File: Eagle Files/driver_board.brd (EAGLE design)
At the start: 127 x 114 mm, 70 parts, among them Q1 TIP32, Q2 TIP32, Q3 TIP32, Q4 TIP32, Q5 TIP32, Q6 TIP32, Q7 TIP32, Q8 TIP32, U1 STP16CPP05MTR, U10 STP16CPP05MTR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

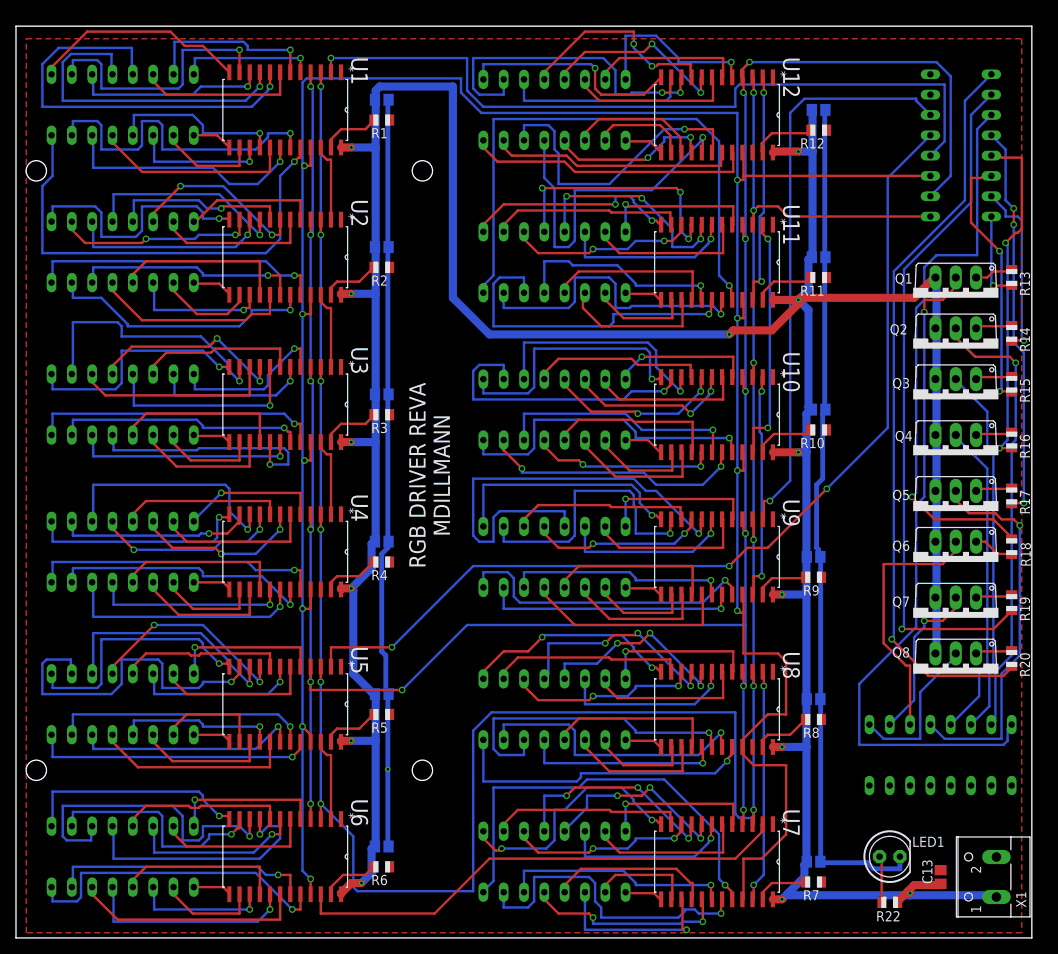
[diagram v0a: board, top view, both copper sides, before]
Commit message: Driver Board - Production Release
final board layout - release for production
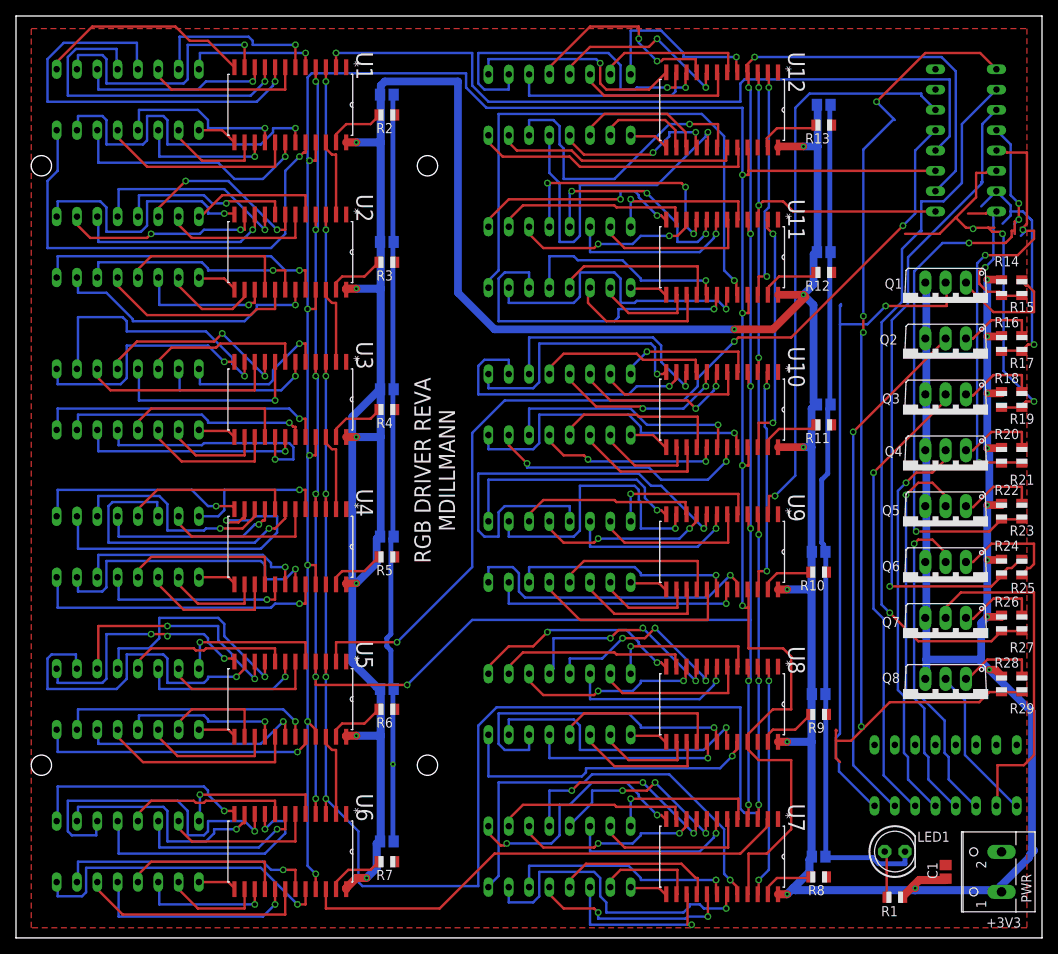
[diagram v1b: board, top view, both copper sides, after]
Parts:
- removed X1: (no value), con-wago-500:W237-102
- added PWR: (no value), con-wago-500:W237-102
- added R21, R23, R25, R27, R29: 1K, adafruit:R0805
- added R24, R26, R28: 2K, adafruit:R0805
- C1: value (none) -> 0.01
- R1: value 1K -> 220
- R13, R15, R17, R19: value 1k -> 1K
- R14, R16, R18, R20: value 1k -> 2K
- R22: value 220 -> 2K
- moved C1 119.5 mm to (116.2, 8.26), flipped to the top, turned to 90 degrees
- moved R1 116.4 mm to (109.9, 5.08), turned to 0 degrees
- moved C13 97.6 mm to (101.0, 104.1), flipped to the bottom, turned to 180 degrees
- moved SV14 78.8 mm to (116.2, 20.3), turned to 180 degrees
- moved SV13 76.9 mm to (118.7, 99.7), turned to 90 degrees
- moved C7 53.4 mm to (46.4, 12.1)
- moved R7 53.4 mm to (46.4, 9.53)
- moved R22 50.9 mm to (123.2, 53.3), turned to 270 degrees
- moved R13 30.2 mm to (101.0, 101.6), turned to 180 degrees
- moved R19 25.4 mm to (125.7, 67.3)
- moved R20 25.4 mm to (123.2, 60.3)
- moved C5 19.7 mm to (46.4, 50.2)
- moved C6 19.7 mm to (46.4, 31.1)
- moved C8 19.7 mm to (100.3, 10.2)
- moved R5 19.7 mm to (46.4, 47.6)
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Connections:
- net +3V3: now also PWR.1, R1.2, R14.1, R16.1, R18.1, R20.1, R22.1, R24.1, R26.1, R28.1; no longer R22.2, X1.1
- net CLK: now also SV13.2; no longer SV14.2
- net GND: now also PWR.2, R13.1; no longer R1.1, X1.2
- net LE: now also SV13.4; no longer SV14.4
- net N$108: now also R7.2; no longer R6.2
- net N$126: now also R8.2; no longer R7.2
- net N$144: now also R9.2; no longer R8.2
- net N$162: now also R10.2; no longer R9.2
- net N$180: now also R11.2; no longer R10.2
- net N$19: now also R2.2; no longer R1.2
- net N$198: now also R12.2; no longer R11.2
- net N$216: now also R13.2; no longer R12.2
- net N$226: now also SV14.1; no longer SV13.1
- net N$227: now also SV14.3; no longer SV13.3
- net N$228: now also SV14.5; no longer SV13.5
- net N$229: now also SV14.7; no longer SV13.7
- net N$230: now also SV14.9; no longer SV13.9
- net N$231: now also SV14.11; no longer SV13.11
- net N$232: now also R15.1; no longer R13.1
- net N$233: now also SV14.13; no longer SV13.13
- net N$234: now also SV14.15; no longer SV13.15
- net N$235: now also R29.1; no longer R20.1
- net N$236: now also R27.1; no longer R19.1
- net N$237: now also R25.1; no longer R18.1
- net N$238: now also R23.1; no longer R17.1
- net N$239: now also R21.1; no longer R16.1
- net N$240: now also R19.1; no longer R15.1
- net N$241: now also R17.1; no longer R14.1
- net N$243: now also R28.2, R29.2, SV13.15; no longer R20.2, SV14.15
- net N$244: now also R1.1; no longer R22.1
- net N$245: now also R26.2, R27.2, SV13.13; no longer R19.2, SV14.13
- net N$246: now also R24.2, R25.2, SV13.11; no longer R18.2, SV14.11
- net N$247: now also R22.2, R23.2, SV13.9; no longer R17.2, SV14.9
- net N$248: now also R20.2, R21.2, SV13.7; no longer R16.2, SV14.7
- net N$249: now also R18.2, R19.2, SV13.5; no longer R15.2, SV14.5
- net N$250: now also R16.2, R17.2, SV13.3; no longer R14.2, SV14.3
- net N$251: now also R14.2, R15.2, SV13.1; no longer R13.2, SV14.1
- net N$36: now also R3.2; no longer R2.2
- net N$54: now also R4.2; no longer R3.2
- net N$72: now also R5.2; no longer R4.2
- net N$90: now also R6.2; no longer R5.2
- net SDI_B: now also SV13.12; no longer SV14.12
- net SDI_G: now also SV13.10; no longer SV14.10
- net SDI_R: now also SV13.8; no longer SV14.8
- net ~OE: now also SV13.6; no longer SV14.6
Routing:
- net +3V3: track 432.1 -> 545.8 mm, vias 14 -> 22
- net N$243: track 93.2 -> 129.8 mm, vias 1 -> 4
- net N$247: track 49.3 -> 78.1 mm, vias 3 -> 4
- net N$233: track 20.6 -> 43.7 mm, vias 1 -> 0
- net N$249: track 32.6 -> 51.2 mm, vias 2 -> 3
- net N$149: track 24.5 -> 42.3 mm
- net N$145: track 21.3 -> 37.3 mm, vias 2 -> 1
- net N$246: track 69.5 -> 83.4 mm
- net N$248: track 43.3 -> 56.5 mm, vias 2 -> 3
- net N$228: track 46.4 -> 57.4 mm, vias 0 -> 1
- net N$229: track 39.7 -> 50.2 mm, vias 0 -> 1
- net N$232: track 5.00 -> 15.1 mm
- net N$231: track 32.6 -> 42.1 mm, vias 0 -> 1
- net N$251: track 11.0 -> 20.2 mm
- net N$227: track 56.5 -> 65.6 mm
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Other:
- board size 127 x 114 mm -> 128.2 x 115.2 mm
- board text added: "+3V3"
